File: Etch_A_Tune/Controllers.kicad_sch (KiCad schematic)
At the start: 7 parts, among them U3 RIC11-31S10K2-GSMT, U4 RIC11-31S10K2-GSMT

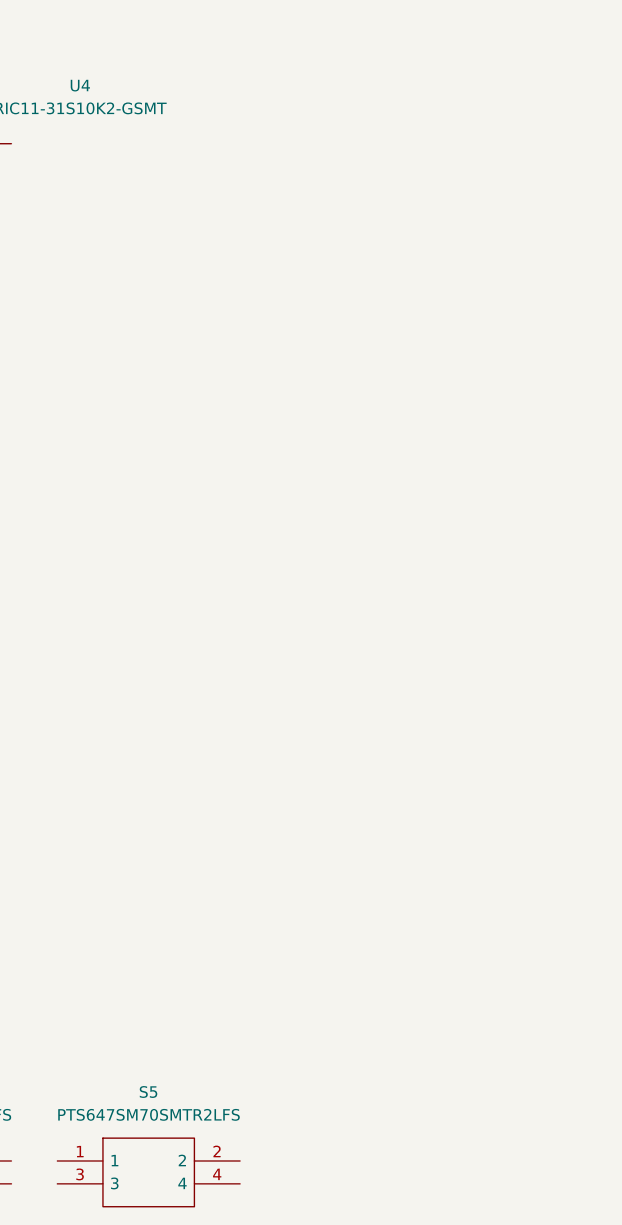
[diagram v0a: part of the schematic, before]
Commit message: Updated schematic and preliminary PCB doc
did rough PCB layout
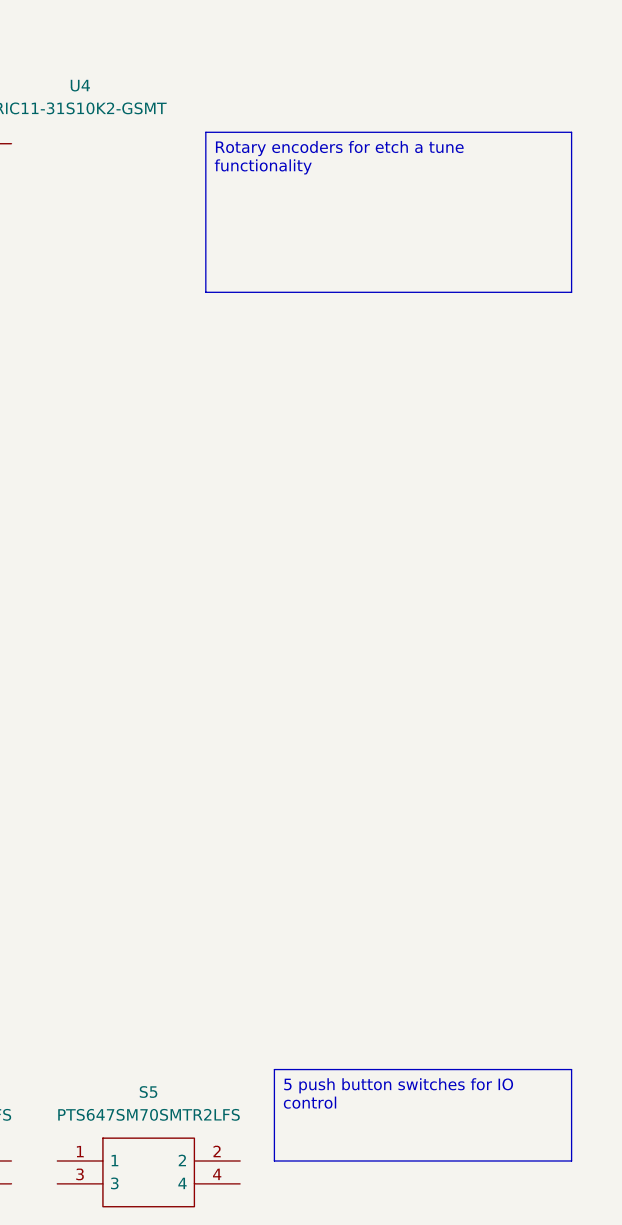
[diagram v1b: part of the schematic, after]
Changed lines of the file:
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@@
 	(generator_version "9.0")
 	(paper "A4")
+	(text_box "5 push button switches for IO control\n"
+		(exclude_from_sim no)
+		(at 195.58 144.78 0)
+		(size 33.02 10.16)
+		(margins 0.9525 0.9525 0.9525 0.9525)
+		(stroke
+			(width 0)
+			(type solid)
+		)
+		(fill
+			(type none)
+		)
+		(effects
+			(font
+				(size 1.27 1.27)
+			)
+			(justify left top)
+		)
+	)
+	(text_box "Rotary encoders for etch a tune functionality"
+		(exclude_from_sim no)
+		(at 187.96 40.64 0)
+		(size 40.64 17.78)
+		(margins 0.9525 0.9525 0.9525 0.9525)
+		(stroke
+			(width 0)
+			(type solid)
+		)
+		(fill
+			(type none)
+		)
+		(effects
+			(font
+				(size 1.27 1.27)
+			)
+			(justify left top)
+		)
+	)
 	(hierarchical_label "SW4"
 		(shape input)

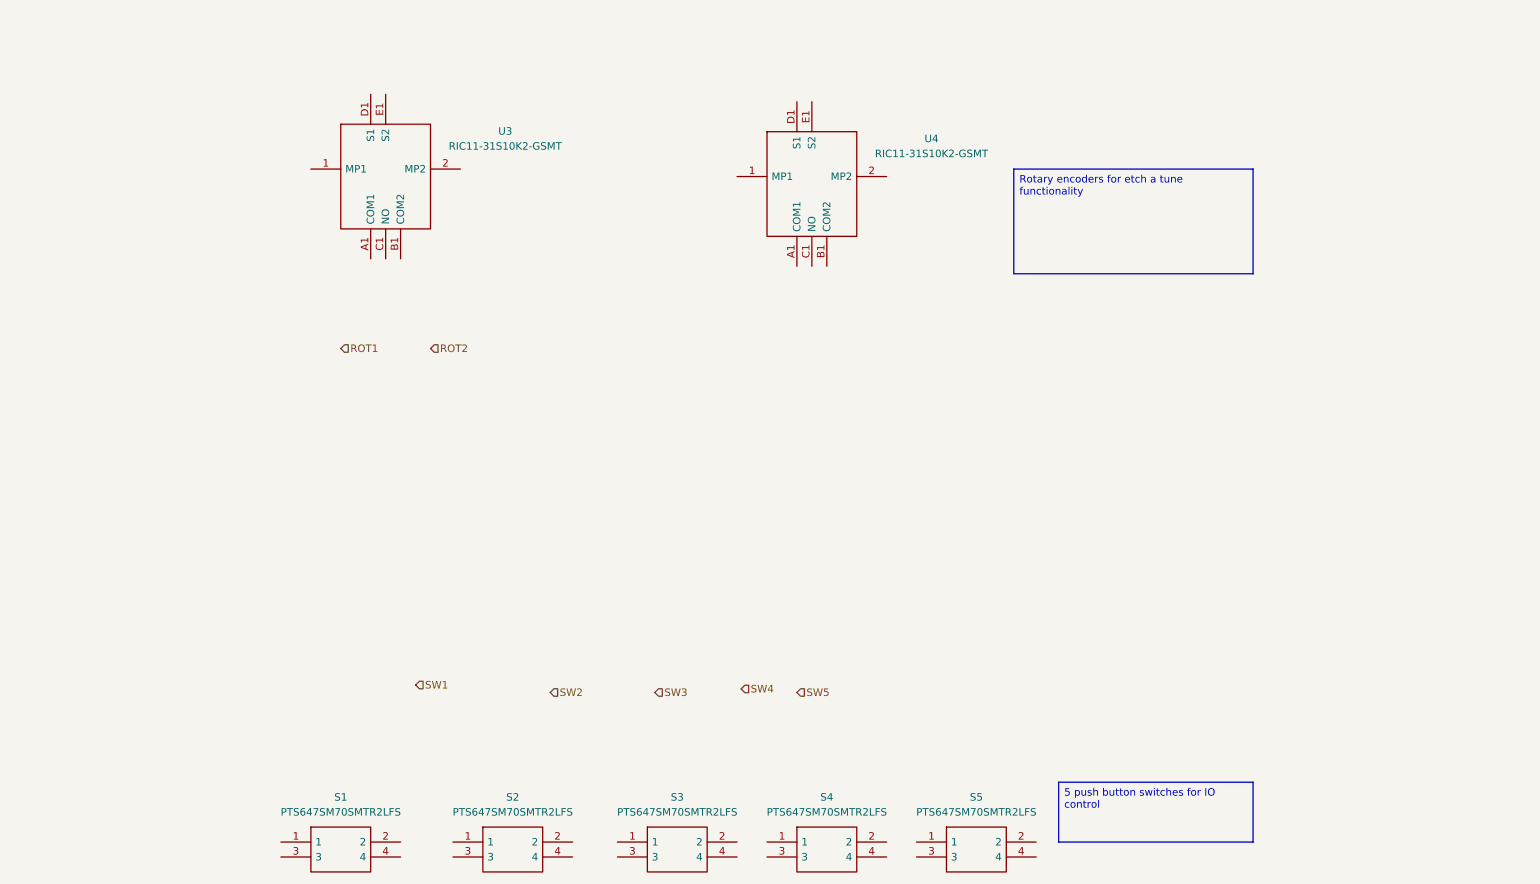
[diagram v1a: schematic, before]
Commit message: Schematic Update
Fixed component Footprints and added new switches/rotary encoders. Wired and placed bypass capacitors for most devices. Removed 5V boost converter because external DAC is no longer being utilized. Placed uC onto board design and implemented charging through USB-C connector.
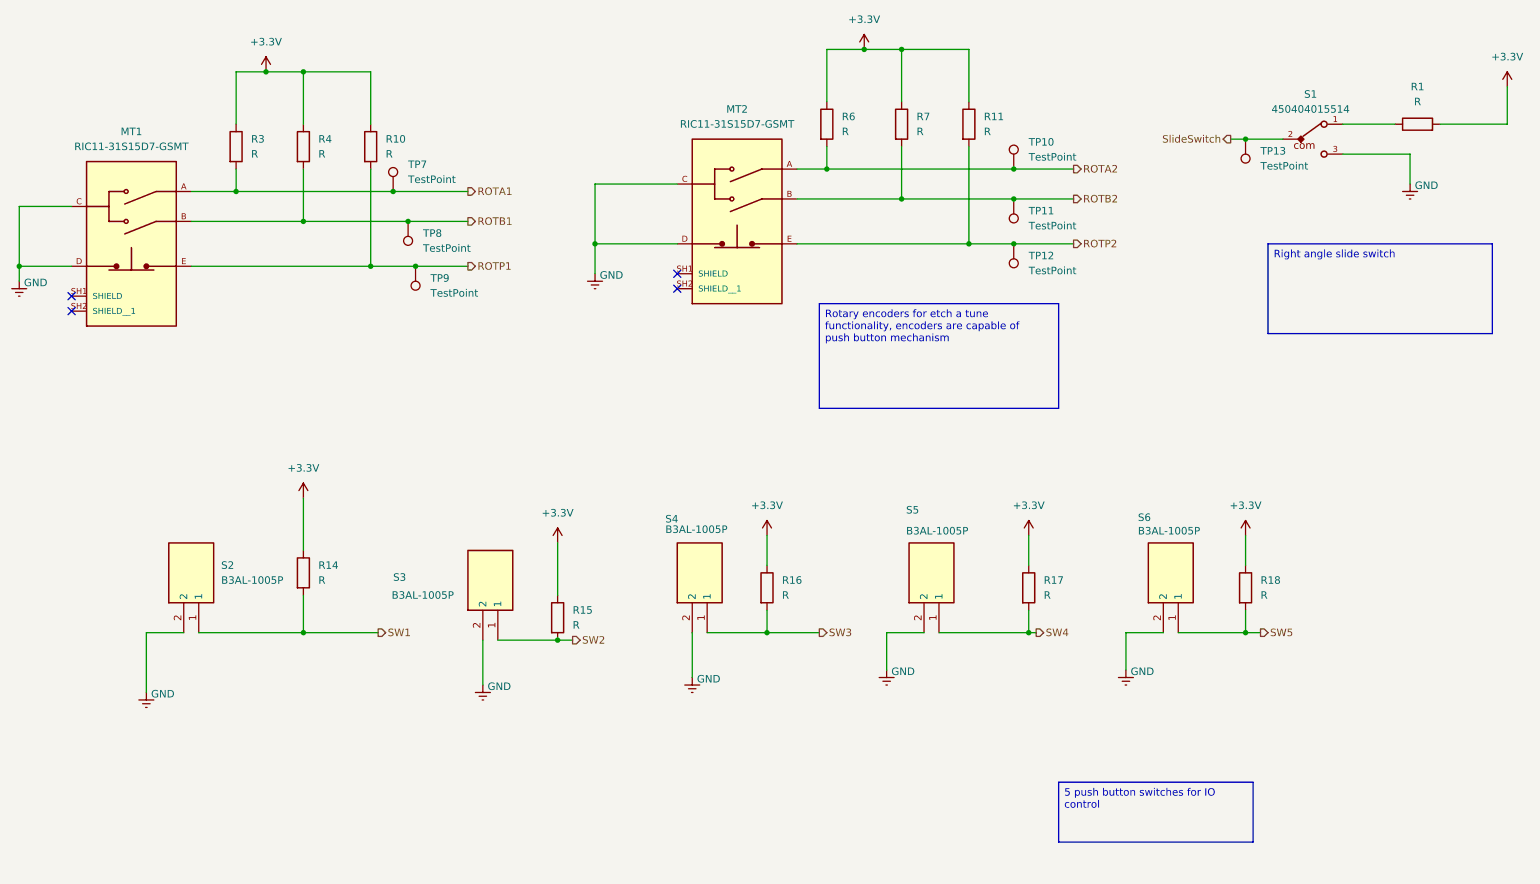
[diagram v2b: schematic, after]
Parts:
- removed S1, S2, S3, S4, S5: PTS647SM70SMTR2LFS, PTS647SM38SMTR2LFS, symbol SamacSys_Parts:PTS647SM70SMTR2LFS
- removed U3, U4: RIC11-31S10K2-GSMT, RIC1131S10K2GSMT, symbol SamacSys_Parts:RIC11-31S10K2-GSMT
- added MT1, MT2: RIC11-31S15D7-GSMT, BQ25170DSGR:XDCR_RIC11-31S15D7-GSMT, symbol RIC11-31S15D7-GSMT:RIC11-31S15D7-GSMT
- added R1, R10, R11, R14, R15, R16, R17, R18, R3, R4, R6, R7: R, symbol Device:R
- added S1: 450404015514, BQ25170DSGR:450404015514, symbol 450404015514:450404015514
- added S2, S3, S4, S5, S6: B3AL-1005P, BQ25170DSGR:B3AL1005P, symbol B3AL-1005P:B3AL-1005P
- added TP10, TP11, TP12, TP13, TP7, TP8, TP9: TestPoint, TestPoint:TestPoint_Pad_D1.0mm, symbol Connector:TestPoint
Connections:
- net SW1: now also R14.2, S2.1
- net SW2: now also R15.2, S3.1
- net SW3: now also R16.2, S4.1
- net SW4: now also R17.2, S5.1
- net SW5: now also R18.2, S6.1
- new net: R1.1, S1.1
- new net +3.3V: R1.2, R10.1, R11.1, R14.1, R15.1, R16.1, R17.1, R18.1, R3.1, R4.1, R6.1, R7.1
- new net GND: MT1.C, MT1.D, MT2.C, MT2.D, S1.3, S2.2, S3.2, S4.2, S5.2, S6.2
- new net ROTA1: MT1.A, R3.2, TP7.1
- new net ROTA2: MT2.A, R6.2, TP10.1
- new net ROTB1: MT1.B, R4.2, TP8.1
- new net ROTB2: MT2.B, R7.2, TP11.1
- new net ROTP1: MT1.E, R10.2, TP9.1
- new net ROTP2: MT2.E, R11.2, TP12.1
- new net SlideSwitch: S1.2, TP13.1
- no-connect marks 0 -> 4

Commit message: Etch A Tune V.02
Updated more foot prints and components onto bom, specifically SWD debug header and 1x14 pin header for touch and screen module. Added 4pin header for SD card reader.
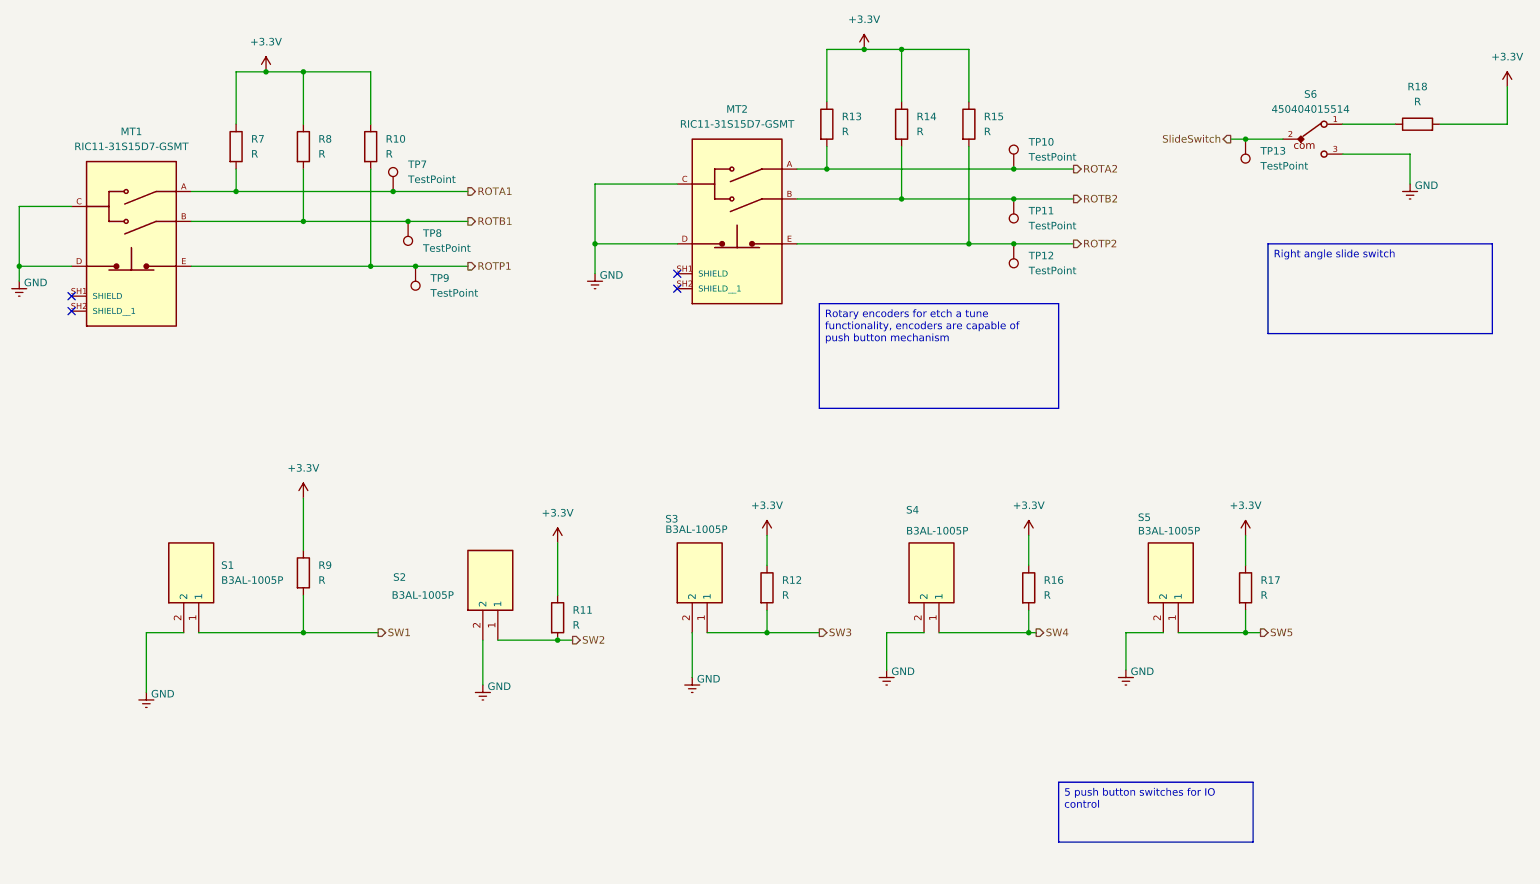
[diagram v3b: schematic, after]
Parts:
- renumbered R15 to R11, R16 to R12, R6 to R13, R7 to R14, R11 to R15, R17 to R16, R18 to R17, R1 to R18, R3 to R7, R4 to R8, R14 to R9, S2 to S1, S3 to S2, S4 to S3, S5 to S4, S6 to S5, S1 to S6

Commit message: Updated parallel power supply
Updated USB and battery operation and added DAC output
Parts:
- added TP14, TP15: TestPoint, TestPoint:TestPoint_Pad_D1.0mm, symbol Connector:TestPoint
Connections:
- net SW1: now also TP14.1
- net SW2: now also TP15.1
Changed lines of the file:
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@@
 	)
 	(junction
+		(at 72.39 119.38)
+		(diameter 0)
+		(color 0 0 0 0)
+	)
+	(junction
 		(at 19.05 57.15)
 		(diameter 0)
@@
 	)
 	(junction
+		(at 119.38 120.65)
+		(diameter 0)
+		(color 0 0 0 0)
+	)
+	(junction
 		(at 180.34 53.34)
 		(diameter 0)
@@
 	(wire
 		(pts
-			(xy 67.31 119.38) (xy 80.01 119.38)
+			(xy 67.31 119.38) (xy 72.39 119.38)
 		)
 		(stroke
@@
 	(wire
 		(pts
+			(xy 72.39 119.38) (xy 80.01 119.38)
+		)
+		(stroke
+			(width 0)
+			(type default)
+		)
+	)
+	(wire
+		(pts
 			(xy 227.33 107.95) (xy 227.33 102.87)
 		)
@@
 	(wire
 		(pts
+			(xy 119.38 120.65) (xy 121.92 120.65)
+		)
+		(stroke
+			(width 0)
+			(type default)
+		)
+	)
+	(wire
+		(pts
 			(xy 82.55 44.45) (xy 95.25 44.45)
 		)
@@
 	(wire
 		(pts
-			(xy 110.49 120.65) (xy 113.03 120.65)
+			(xy 110.49 120.65) (xy 119.38 120.65)
 		)
 		(stroke
@@
 	(hierarchical_label "SW2"
 		(shape output)
-		(at 113.03 120.65 0)
+		(at 121.92 120.65 0)
 		(effects
 			(font
@@
 	)
 	(symbol
+		(lib_id "Connector:TestPoint")
+		(at 119.38 120.65 0)
+		(mirror y)
+		(unit 1)
+		(exclude_from_sim no)
+		(in_bom yes)
+		(on_board yes)
+		(dnp no)
+		(property "Reference" "TP15"
+			(at 121.92 118.6181 0)
+			(effects
+				(font
+					(size 1.27 1.27)
+				)
+				(justify right)
+			)
+		)
+		(property "Value" "TestPoint"
+			(at 121.92 116.0781 0)
+			(effects
+				(font
+					(size 1.27 1.27)
+				)
+				(justify right)
+			)
+		)
+		(property "Footprint" "TestPoint:TestPoint_Pad_D1.0mm"
+			(at 114.3 120.65 0)
+			(effects
+				(font
+					(size 1.27 1.27)
+				)
+				(hide yes)
+			)
+		)
+		(property "Datasheet" "~"
+			(at 114.3 120.65 0)
+			(effects
+				(font
+					(size 1.27 1.27)
+				)
+				(hide yes)
+			)
+		)
+		(property "Description" "test point"
+			(at 119.38 120.65 0)
+			(effects
+				(font
+					(size 1.27 1.27)
+				)
+				(hide yes)
+			)
+		)
+		(pin "1"
+		)
+		(instances
+			(project "Etch_A_Tune"
+				(path "/b4cdadf2-c4fe-48fe-ba6a-e15d1cad03b2/85ce9e3c-81ec-4c89-ba57-7d8ff70f58fc"
+					(reference "TP15")
+					(unit 1)
+				)
+			)
+		)
+	)
+	(symbol
 		(lib_id "power:+3.3V")
 		(at 271.78 26.67 0)
@@
 					(unit 1)
 				)
+			)
+		)
+	)
+	(symbol
+		(lib_id "Connector:TestPoint")
+		(at 72.39 119.38 0)
+		(mirror y)
+		(unit 1)
+		(exclude_from_sim no)
+		(in_bom yes)
+		(on_board yes)
+		(dnp no)
+		(property "Reference" "TP14"
+			(at 74.93 117.3481 0)
+			(effects
+				(font
+					(size 1.27 1.27)
+				)
+				(justify right)
+			)
+		)
+		(property "Value" "TestPoint"
+			(at 74.93 114.8081 0)
+			(effects
+				(font
+					(size 1.27 1.27)
+				)
+				(justify right)
+			)
+		)
+		(property "Footprint" "TestPoint:TestPoint_Pad_D1.0mm"
+			(at 67.31 119.38 0)
+			(effects
+				(font
+					(size 1.27 1.27)
+				)
+				(hide yes)
+			)
+		)
+		(property "Datasheet" "~"
+			(at 67.31 119.38 0)
+			(effects
+				(font
+					(size 1.27 1.27)
+				)
+				(hide yes)
+			)
+		)
+		(property "Description" "test point"
+			(at 72.39 119.38 0)
+			(effects
+				(font
+					(size 1.27 1.27)
+				)
+				(hide yes)
+			)
+		)
+		(pin "1"
+		)
+		(instances
+			(project "Etch_A_Tune"
+				(path "/b4cdadf2-c4fe-48fe-ba6a-e15d1cad03b2/85ce9e3c-81ec-4c89-ba57-7d8ff70f58fc"
+					(reference "TP14")
+					(unit 1)
+				)

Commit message: Final Layout before routing
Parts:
- R10, R11, R12, R13, R14, R15, R16, R17, R18, R7, R8, R9: value R -> 10k; footprint (none) -> Resistor_SMD:R_0603_1608Metric
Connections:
- net +3.3V: now also R18.1; no longer R18.2
- net at S6.1: now also R18.2; no longer R18.1

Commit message: Another Update! :D
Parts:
- renumbered R7 to R25, R8 to R26, R9 to R27, R10 to R28, R11 to R29, R12 to R30, R13 to R31, R14 to R32, R15 to R33, R16 to R34, R17 to R35, R18 to R36, TP14 to TP30, TP7 to TP31, TP8 to TP32, TP9 to TP33, TP15 to TP34, TP10 to TP35, TP11 to TP36, TP12 to TP37, TP13 to TP38

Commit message: pdf docs
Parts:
- renumbered R28 to R10, R29 to R11, R30 to R12, R31 to R13, R32 to R14, R33 to R15, R34 to R16, R35 to R17, R36 to R18, R25 to R7, R26 to R8, R27 to R9, TP35 to TP10, TP36 to TP11, TP37 to TP12, TP38 to TP13, TP30 to TP14, TP34 to TP15, TP31 to TP7, TP32 to TP8, TP33 to TP9

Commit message: Updated BOM
Changed Values for an accurate BOM, and exported results
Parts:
- MT1, MT2: DIGIKEY-PURCHASE-URL (none) -> https://www.digikey.com/short/wwz34c7b; Dist (none) -> Digikey; Dist Part Number (none) -> 2223-RIC11-31S15D7-GSMT-ND; Manufacturer_Name (none) -> Same Sky (Formerly CUI Devices); Manufacturer_Part_Number (none) -> RIC11-31S15D7-GSMT; Price (none) -> $2.14
- R10, R11, R12, R13, R14, R15, R16, R17, R18, R7, R8, R9: DIGIKEY-PURCHASE-URL (none) -> https://www.digikey.com/short/m3dw570p; Dist (none) -> Digikey; Dist Part Number (none) -> 311-10.0KHRCT-ND; Manufacturer_Name (none) -> YAGEO; Manufacturer_Part_Number (none) -> RC0603FR-0710KL; Price (none) -> $0.10
- S1, S2, S3, S4, S5: DIGIKEY-PURCHASE-URL (none) -> https://www.digikey.com/short/bf0nw4cm; Dist (none) -> Digikey; Dist Part Number (none) -> Z7816CT-ND; Price (none) -> $1.53
- S6: DIGIKEY-PURCHASE-URL (none) -> https://www.digikey.com/short/1n58hc8b; Dist (none) -> Digikey; Dist Part Number (none) -> 732-13665-1-ND; Manufacturer_Name (none) -> Würth Elektronik; Manufacturer_Part_Number (none) -> 450404015514; Price (none) -> $0.80
- TP10, TP11, TP12, TP13, TP14, TP15, TP7, TP8, TP9: Dist (none) -> Digikey; now left out of the parts list
